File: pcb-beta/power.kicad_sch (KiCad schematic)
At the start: 11 parts, among them U1 MIC5335-JGYMT, U2 NCP163AFCT180T2G

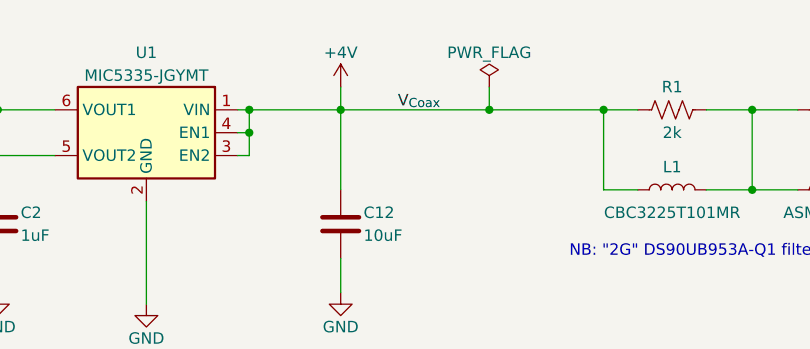
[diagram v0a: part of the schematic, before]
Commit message: Move pcb to pcb-beta directory
- Because this board only works with Beta-test NP2.0 probes
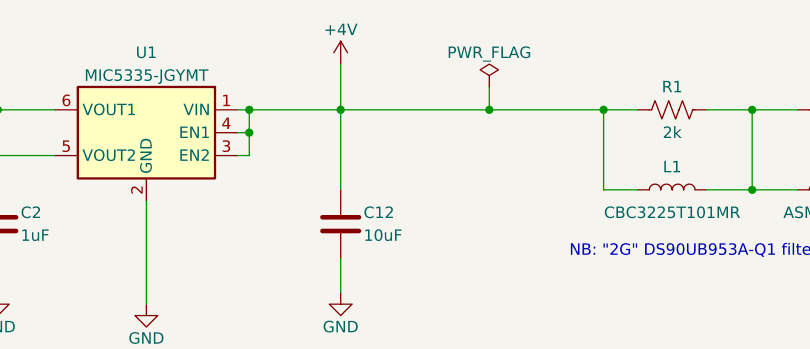
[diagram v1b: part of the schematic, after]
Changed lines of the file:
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@@
     (stroke (width 0) (type default))
   )
-  (wire (pts (xy 152.4 60.96) (xy 152.4 63.5))
+  (wire (pts (xy 152.4 58.42) (xy 152.4 63.5))
     (stroke (width 0) (type default))
   )
@@
   )
   (text "NB: \"2G\" DS90UB953A-Q1 filter network." (at 177.8 80.01 0)
-    (effects (font (size 1.27 1.27)) (justify left bottom))
-  )
-  (label "V_{Coax}" (at 158.75 63.5 0) (fields_autoplaced)
     (effects (font (size 1.27 1.27)) (justify left bottom))
   )
@@
     )
   )
-  (symbol (lib_id "power:+4V") (at 152.4 60.96 0) (unit 1)
+  (symbol (lib_id "power:+4V") (at 152.4 58.42 0) (unit 1)
     (in_bom yes) (on_board yes) (dnp no) (fields_autoplaced)
-    (property "Reference" "#PWR05" (at 152.4 64.77 0)
-      (effects (font (size 1.27 1.27)) hide)
-    )
-    (property "Value" "+4V" (at 152.4 57.15 0)
-      (effects (font (size 1.27 1.27)))
-    )
-    (property "Footprint" "" (at 152.4 60.96 0)
-      (effects (font (size 1.27 1.27)) hide)
-    )
-    (property "Datasheet" "" (at 152.4 60.96 0)
-      (effects (font (size 1.27 1.27)) hide)
-    )
+    (property "Reference" "#PWR05" (at 152.4 62.23 0)
+      (effects (font (size 1.27 1.27)) hide)
+    )
+    (property "Value" "+4V" (at 152.4 54.61 0)
+      (effects (font (size 1.27 1.27)))
+    )
+    (property "Footprint" "" (at 152.4 58.42 0)
+      (effects (font (size 1.27 1.27)) hide)
+    )
+    (property "Datasheet" "" (at 152.4 58.42 0)
+      (effects (font (size 1.27 1.27)) hide)
+    )
